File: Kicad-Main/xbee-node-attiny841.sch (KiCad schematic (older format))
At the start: 40 parts, among them P10 CONN_1, P11 CONN_1, P12 CONN_1, P13 CONN_1, P14 CONN_1, P15 CONN_1, P16 CONN_1, P17 CONN_1, P18 CONN_1, P2 XBee Adaptor, P3 Test, P4 Battery, P5 XBee-ext-1, P6 XBee-ext-2, P7 CONN_1, P8 CONN_1, P9 CONN_1, Q2 S9014, Q3 2N7000, U1 ATTINY84-S, U2 MAX952ESA, U3 TPS77033

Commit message: Changes made by Kicad following upstream library changes
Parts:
- C1, C2, C4, C6, C7, C8, C9: symbol C -> C-RESCUE-xbee-node-attiny841
- C3: symbol CP -> CP-RESCUE-xbee-node-attiny841
- D1: symbol LED -> LED-RESCUE-xbee-node-attiny841
- Q2: symbol NPN -> NPN-RESCUE-xbee-node-attiny841
- Q3: symbol MOSFET_N -> MOSFET_N-RESCUE-xbee-node-attiny841
- R1, R2, R5, R6, R7, R8, R9: symbol R -> R-RESCUE-xbee-node-attiny841
- U2: symbol LM358 -> LM358-RESCUE-xbee-node-attiny841
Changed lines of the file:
@@
 EESchema Schematic File Version 2
+LIBS:xbee-node-attiny841-rescue
 LIBS:power
 LIBS:device
@@
 LIBS:Sensors
 LIBS:xbee-node-attiny841-cache
-EELAYER 24 0
+EELAYER 25 0
 EELAYER END
 $Descr A4 11693 8268
@@
 $EndComp
 $Comp
-L MOSFET_N Q3
+L MOSFET_N-RESCUE-xbee-node-attiny841 Q3
 U 1 1 53D32AE5
 P 9550 2700
@@
 $EndComp
 $Comp
-L R R7
+L R-RESCUE-xbee-node-attiny841 R7
 U 1 1 53D32AFA
 P 9650 2250
@@
 $EndComp
 $Comp
-L R R8
+L R-RESCUE-xbee-node-attiny841 R8
 U 1 1 53D32B0E
 P 9650 3150
@@
 $EndComp
 $Comp
-L R R6
+L R-RESCUE-xbee-node-attiny841 R6
 U 1 1 53D32B68
 P 2950 2900
@@
 $EndComp
 $Comp
-L CP C3
+L CP-RESCUE-xbee-node-attiny841 C3
 U 1 1 53D32BEA
 P 6150 1750
@@
 $EndComp
 $Comp
-L GND #PWR01
+L GND-RESCUE-xbee-node-attiny841 #PWR01
 U 1 1 53D32D54
 P 3850 3650
@@
 $EndComp
 $Comp
-L C C2
+L C-RESCUE-xbee-node-attiny841 C2
 U 1 1 53D32ECC
 P 5400 1750
@@
 $EndComp
 $Comp
-L GND #PWR03
+L GND-RESCUE-xbee-node-attiny841 #PWR03
 U 1 1 53D32F27
 P 5400 1950
@@
 $EndComp
 $Comp
-L GND #PWR04
+L GND-RESCUE-xbee-node-attiny841 #PWR04
 U 1 1 53D32F3B
 P 6150 1950
@@
 $EndComp
 $Comp
-L GND #PWR05
+L GND-RESCUE-xbee-node-attiny841 #PWR05
 U 1 1 53D33037
 P 2950 3550
@@
 $EndComp
 $Comp
-L GND #PWR07
+L GND-RESCUE-xbee-node-attiny841 #PWR07
 U 1 1 53D331C5
 P 9650 3400
@@
 $EndComp
 $Comp
-L GND #PWR09
+L GND-RESCUE-xbee-node-attiny841 #PWR09
 U 1 1 53D354FE
 P 6600 1900
@@
 $EndComp
 $Comp
-L GND #PWR010
+L GND-RESCUE-xbee-node-attiny841 #PWR010
 U 1 1 53D35512
 P 6900 1650
@@
 $EndComp
 $Comp
-L LM358 U2
+L LM358-RESCUE-xbee-node-attiny841 U2
 U 2 1 53D35B75
 P 5450 5250
@@
 $EndComp
 $Comp
-L GND #PWR012
+L GND-RESCUE-xbee-node-attiny841 #PWR012
 U 1 1 53D35BB6
 P 5350 5650
@@
 $EndComp
 $Comp
-L R R5
+L R-RESCUE-xbee-node-attiny841 R5
 U 1 1 53D35C63
 P 5300 4500
@@
 $EndComp
 $Comp
-L NPN Q2
+L NPN-RESCUE-xbee-node-attiny841 Q2
 U 1 1 53D35E04
 P 4000 6050
@@
 $EndComp
 $Comp
-L R R2
+L R-RESCUE-xbee-node-attiny841 R2
 U 1 1 53D35F1D
 P 4100 4700
@@
 $EndComp
 $Comp
-L GND #PWR013
+L GND-RESCUE-xbee-node-attiny841 #PWR013
 U 1 1 53D35FD0
 P 4100 6250
@@
 $EndComp
 $Comp
-L C C4
+L C-RESCUE-xbee-node-attiny841 C4
 U 1 1 53D36D73
 P 7300 1600
@@
 $EndComp
 $Comp
-L GND #PWR014
+L GND-RESCUE-xbee-node-attiny841 #PWR014
 U 1 1 53D36D79
 P 7300 1800
@@
 $EndComp
 $Comp
-L GND #PWR015
+L GND-RESCUE-xbee-node-attiny841 #PWR015
 U 1 1 53DCC533
 P 2950 6250
@@
 $EndComp
 $Comp
-L LED D1
+L LED-RESCUE-xbee-node-attiny841 D1
 U 1 1 53DCC508
 P 2950 5350
@@
 $EndComp
 $Comp
-L R R1
+L R-RESCUE-xbee-node-attiny841 R1
 U 1 1 53DCC4A4
 P 2950 4700
@@
 Reset
 $Comp
-L C C1
+L C-RESCUE-xbee-node-attiny841 C1
 U 1 1 53DF7E14
 P 2950 3350
@@
 $EndComp
 $Comp
-L GND #PWR016
+L GND-RESCUE-xbee-node-attiny841 #PWR016
 U 1 1 53E0741A
 P 7000 5900
@@
 $EndComp
 $Comp
-L LM358 U2
+L LM358-RESCUE-xbee-node-attiny841 U2
 U 1 1 53E22CCA
 P 5450 6350
@@
 $EndComp
 $Comp
-L GND #PWR018
+L GND-RESCUE-xbee-node-attiny841 #PWR018
 U 1 1 53E22E2A
 P 5350 6750
@@
 $EndComp
 $Comp
-L GND #PWR019
+L GND-RESCUE-xbee-node-attiny841 #PWR019
 U 1 1 53E22E4B
 P 4950 6450
@@
 NoConn ~ 5950 6350
 $Comp
-L GND #PWR020
+L GND-RESCUE-xbee-node-attiny841 #PWR020
 U 1 1 53E232E1
 P 4950 6250
@@
 Reset
 $Comp
-L GND #PWR021
+L GND-RESCUE-xbee-node-attiny841 #PWR021
 U 1 1 53E22A19
 P 7000 4950
@@
 $EndComp
 $Comp
-L GND #PWR022
+L GND-RESCUE-xbee-node-attiny841 #PWR022
 U 1 1 53E26458
 P 9950 1500
@@
 NoConn ~ 7500 4850
 $Comp
-L C C6
+L C-RESCUE-xbee-node-attiny841 C6
 U 1 1 53E234F0
 P 4150 1750
@@
 $EndComp
 $Comp
-L GND #PWR024
+L GND-RESCUE-xbee-node-attiny841 #PWR024
 U 1 1 53E234F6
 P 4150 1950
@@
 $EndComp
 $Comp
-L C C7
+L C-RESCUE-xbee-node-attiny841 C7
 U 1 1 53E2395C
 P 5900 1750
@@
 $EndComp
 $Comp
-L GND #PWR025
+L GND-RESCUE-xbee-node-attiny841 #PWR025
 U 1 1 53E2398F
 P 5900 1950
@@
 $EndComp
 $Comp
-L GND #PWR026
+L GND-RESCUE-xbee-node-attiny841 #PWR026
 U 1 1 53F32D83
 P 7900 2150
@@
 $EndComp
 $Comp
-L GND #PWR027
+L GND-RESCUE-xbee-node-attiny841 #PWR027
 U 1 1 53F32DAC
 P 8050 2150
@@
 $EndComp
 $Comp
-L GND #PWR028
+L GND-RESCUE-xbee-node-attiny841 #PWR028
 U 1 1 53F2D923
 P 7550 2550
@@
 $EndComp
 $Comp
-L GND #PWR029
+L GND-RESCUE-xbee-node-attiny841 #PWR029
 U 1 1 53F2D950
 P 7700 2550
@@
 $EndComp
 $Comp
-L GND #PWR030
+L GND-RESCUE-xbee-node-attiny841 #PWR030
 U 1 1 53F2D99F
 P 7850 2550
@@
 $EndComp
 $Comp
-L GND #PWR031
+L GND-RESCUE-xbee-node-attiny841 #PWR031
 U 1 1 53F2D9CC
 P 8000 2550
@@
 $EndComp
 $Comp
-L GND #PWR032
+L GND-RESCUE-xbee-node-attiny841 #PWR032
 U 1 1 53F2DC2E
 P 8200 2550
@@
 $EndComp
 $Comp
-L GND #PWR033
+L GND-RESCUE-xbee-node-attiny841 #PWR033
 U 1 1 53F2DC5D
 P 8350 2550
@@
 $EndComp
 $Comp
-L GND #PWR034
+L GND-RESCUE-xbee-node-attiny841 #PWR034
 U 1 1 53F2DFE3
 P 8500 2550
@@
 $EndComp
 $Comp
-L GND #PWR035
+L GND-RESCUE-xbee-node-attiny841 #PWR035
 U 1 1 53FEF658
 P 8950 5100
@@
 $EndComp
 $Comp
-L R R9
+L R-RESCUE-xbee-node-attiny841 R9
 U 1 1 54823620
 P 7000 3000
@@
 $EndComp
 $Comp
-L GND #PWR036
+L GND-RESCUE-xbee-node-attiny841 #PWR036
 U 1 1 5482395B
 P 7000 3250
@@
 $EndComp
 $Comp
-L C C8
+L C-RESCUE-xbee-node-attiny841 C8
 U 1 1 548D0F6B
 P 5100 1750
@@
 $EndComp
 $Comp
-L GND #PWR037
+L GND-RESCUE-xbee-node-attiny841 #PWR037
 U 1 1 548D0F71
 P 5100 1950
@@
 $EndComp
 $Comp
-L C C9
+L C-RESCUE-xbee-node-attiny841 C9
 U 1 1 548D1179
 P 4450 1750
@@
 $EndComp
 $Comp
-L GND #PWR038
+L GND-RESCUE-xbee-node-attiny841 #PWR038
 U 1 1 548D117F
 P 4450 1950

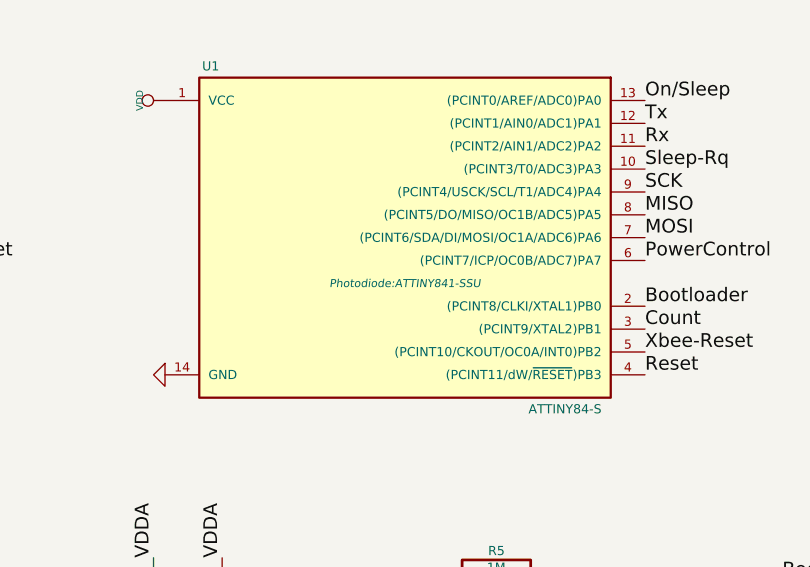
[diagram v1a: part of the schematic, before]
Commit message: Fix minor problems with files to reference provided local libraries. Updates to some documents
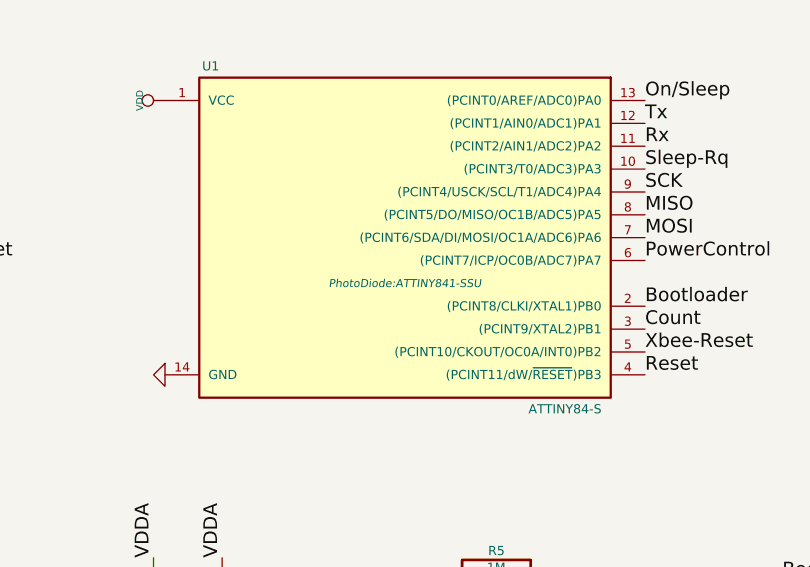
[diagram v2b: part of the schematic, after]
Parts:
- D2: footprint Photodiode:S1133TH -> PhotoDiode:S1133TH
- P12, P13, P14, P15, P16, P17, P18: footprint Photodiode:THROUGHVIA -> PhotoDiode:THROUGHVIA
- P5, P6: footprint Photodiode:pin_header_2mm_1x3 -> PhotoDiode:pin_header_2mm_1x3
- U1: footprint Photodiode:ATTINY841-SSU -> PhotoDiode:ATTINY841-SSU

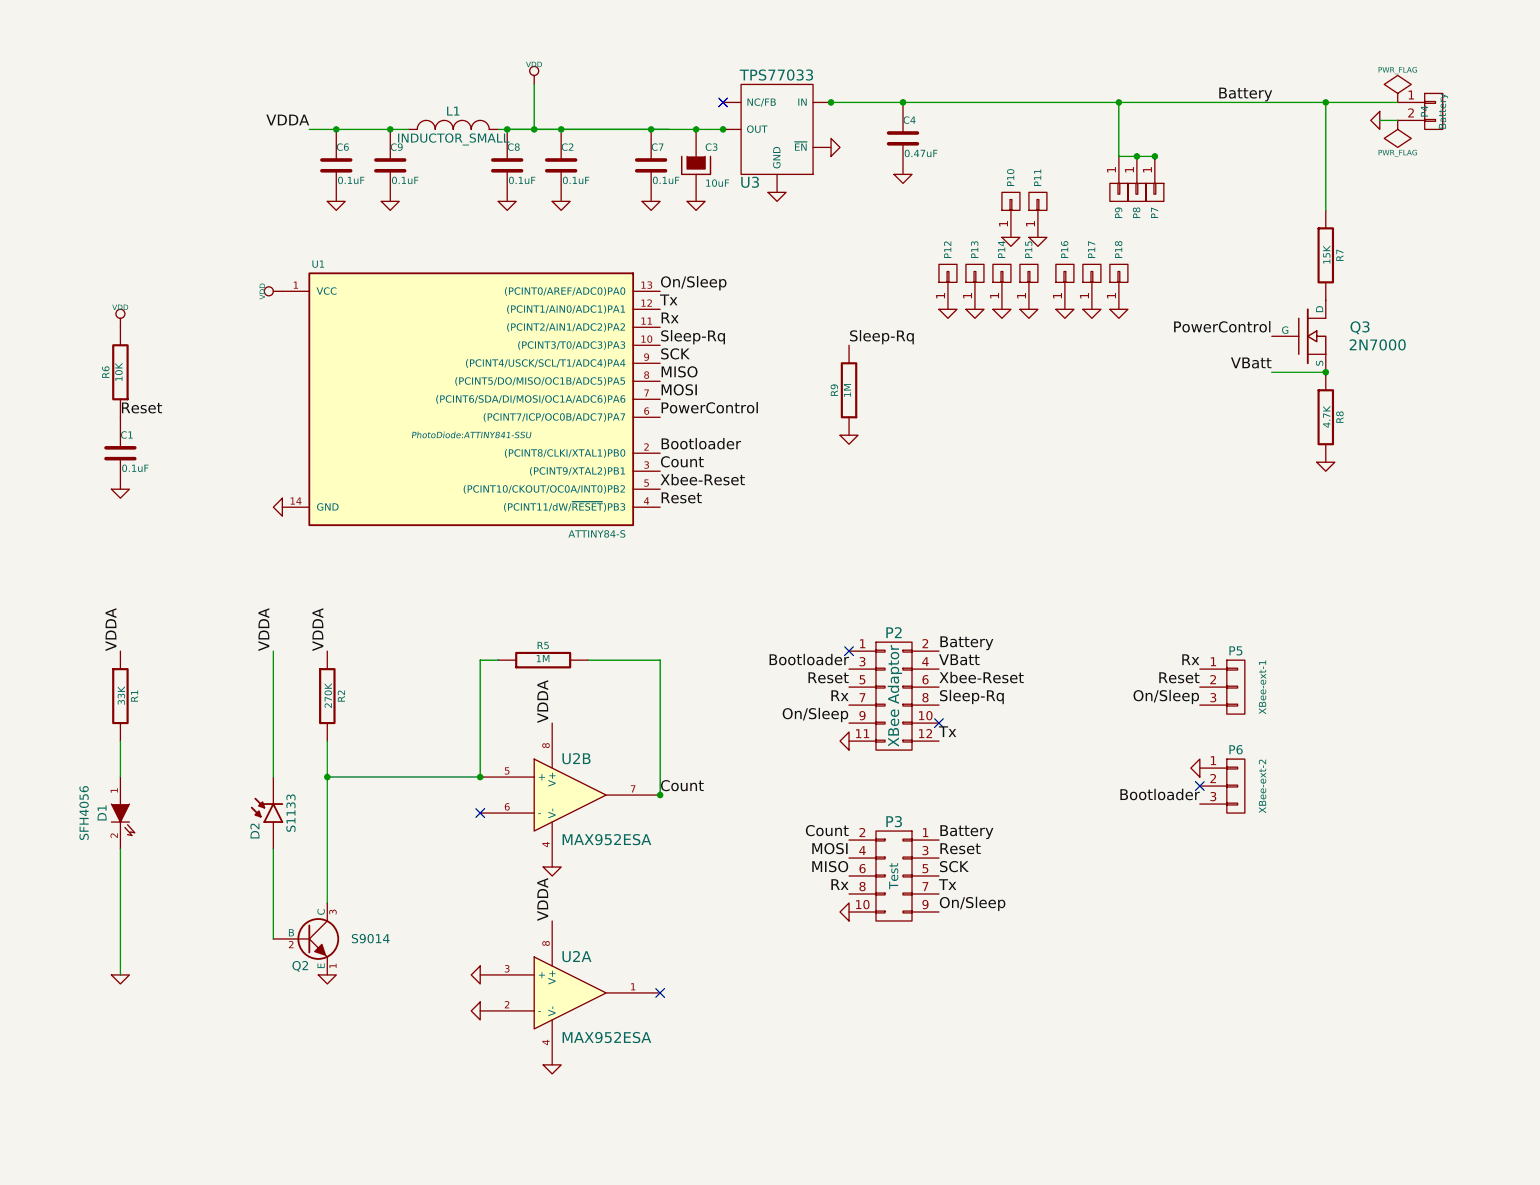
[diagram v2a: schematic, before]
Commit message: Modified both Main and Mounts PCBs to have all footprints in the local library Photodiode.pretty. Saved footprints already in the PCB hopefully avoiding invalidating the PCB in future. Minor changes to schematic and KICAD_SETUP.md
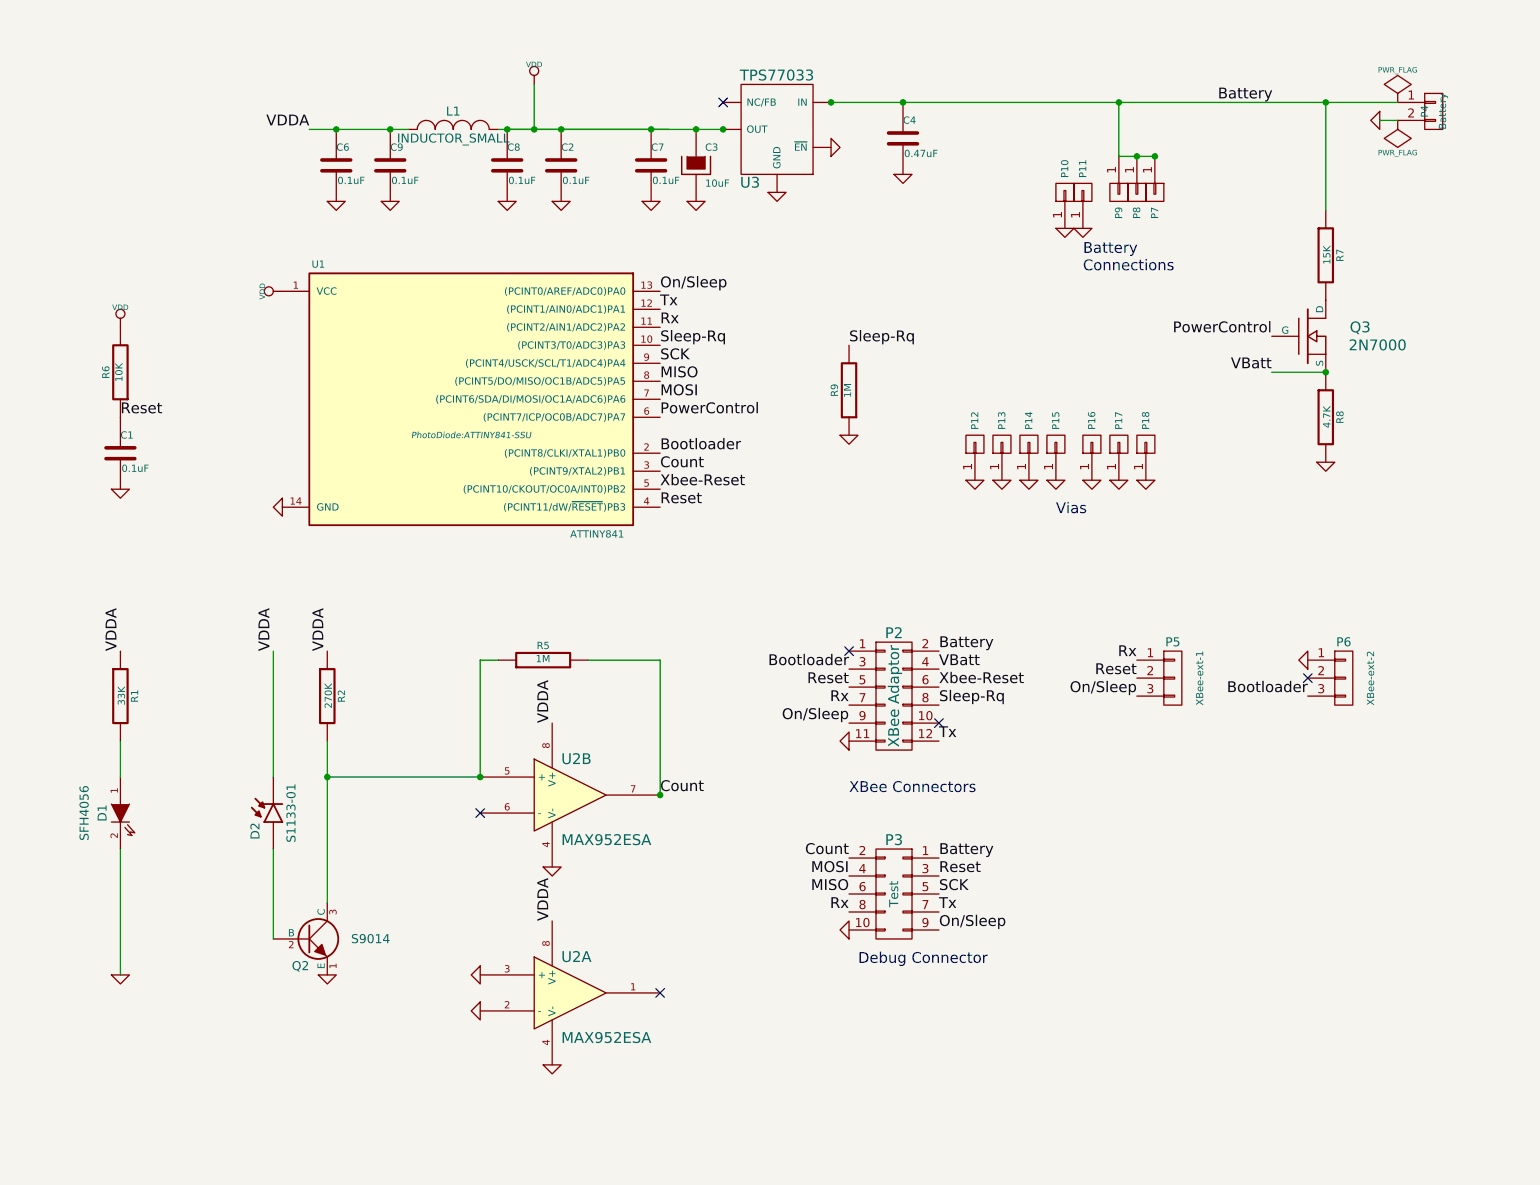
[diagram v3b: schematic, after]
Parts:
- C1, C2, C4, C6, C7: footprint SMD_Packages:SM0603_Capa -> PhotoDiode:SM0603_Capa
- C3: footprint SMD_Packages:SM1206POL -> PhotoDiode:SM1206POL
- C8, C9: footprint SMD_Packages:SMD-0603_c -> PhotoDiode:SM0603_Capa
- D2: value S1133 -> S1133-01
- L1: footprint Resistors_SMD:R_0603 -> PhotoDiode:SM0603_Resistor
- P10, P11, P7, P8, P9: footprint Connect:SIL-1 -> PhotoDiode:SIL-1
- P4: footprint Connect:SIL-2 -> PhotoDiode:SIL-2
- Q2: footprint SMD_Packages:SOT23EBC -> PhotoDiode:SOT23EBC
- Q3: footprint SMD_Packages:SOT23GDS -> PhotoDiode:SOT23GDS
- R1, R2, R5, R6, R7, R8, R9: footprint SMD_Packages:SM0603_Resistor -> PhotoDiode:SM0603_Resistor
- U1: value ATTINY84-S -> ATTINY841
- U2: footprint SMD_Packages:SO8N -> PhotoDiode:SO8N
- U3: footprint SMD_Packages:SOT23-5 -> PhotoDiode:SOT23-5
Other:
- note added: "Battery\nConnections"
- note added: "Debug Connector"
- note added: "Vias"
- note added: "XBee Connectors"
- moved on the sheet: P10, P11, P12, P13, P14, P15, P16, P17, P18, P3, P5, P6
